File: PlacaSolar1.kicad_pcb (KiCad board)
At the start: 2 copper layers, 32 parts, among them J1 Jack-DC, J2 Conn_01x03_Female, J3 Conn_01x06_Female, J4 Conn_01x15_Female, J5 Conn_01x15_Female, SW1 SW_SPDT, SW2 SW_Push, U1 L78L05_SO8

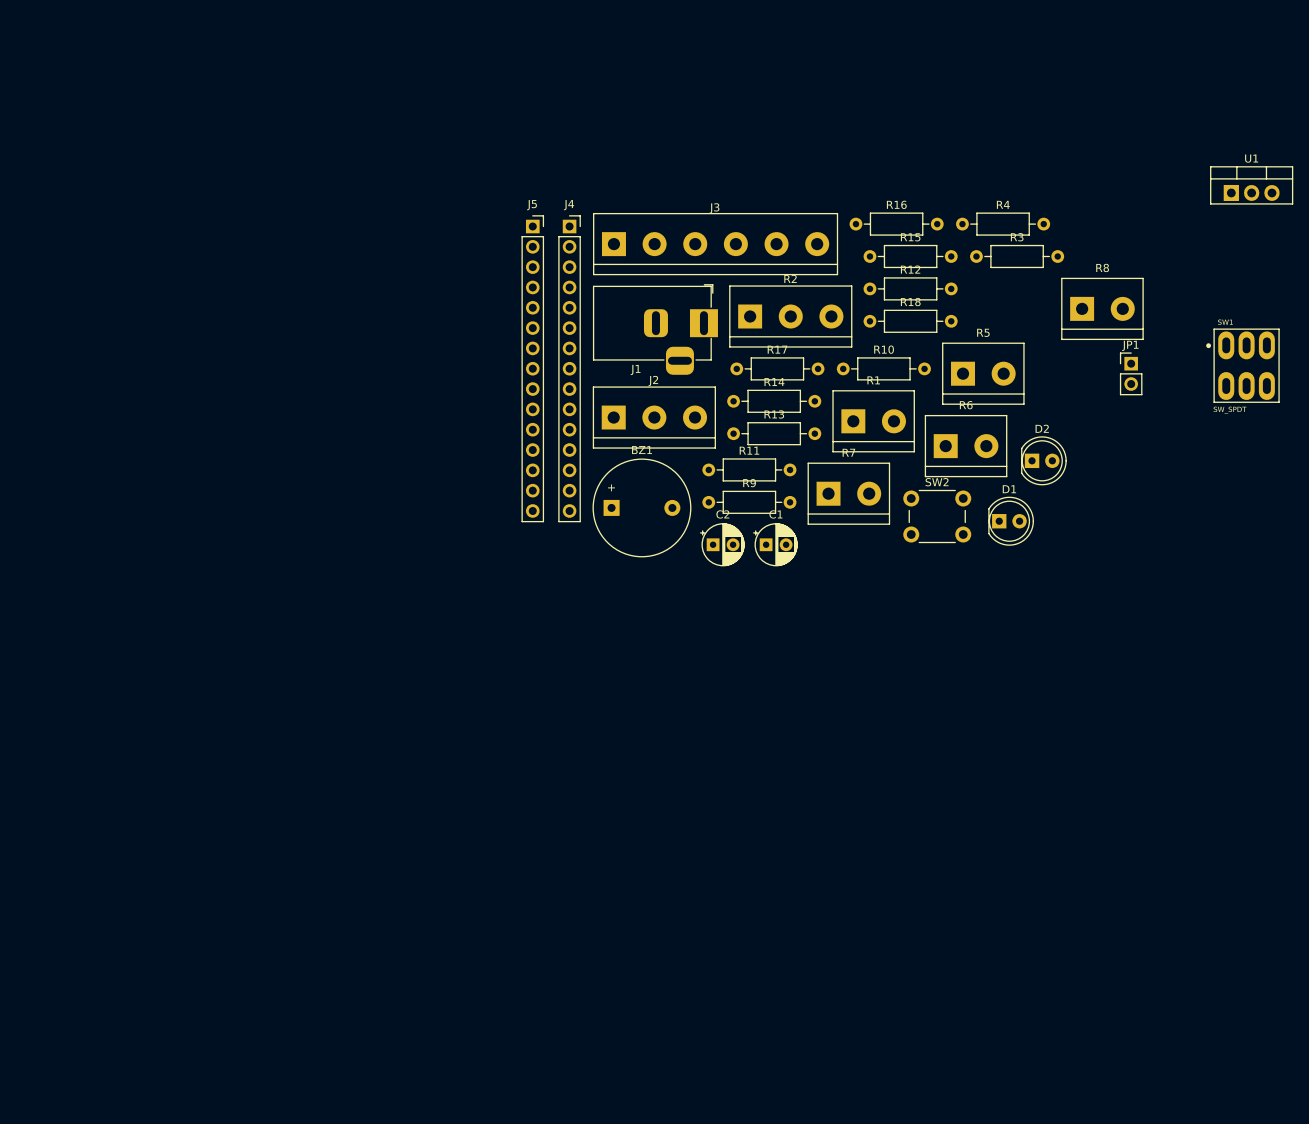
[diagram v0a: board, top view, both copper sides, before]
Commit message: Adicionando modelos 3d, falta o modelo dos bornes, inicio da PCB
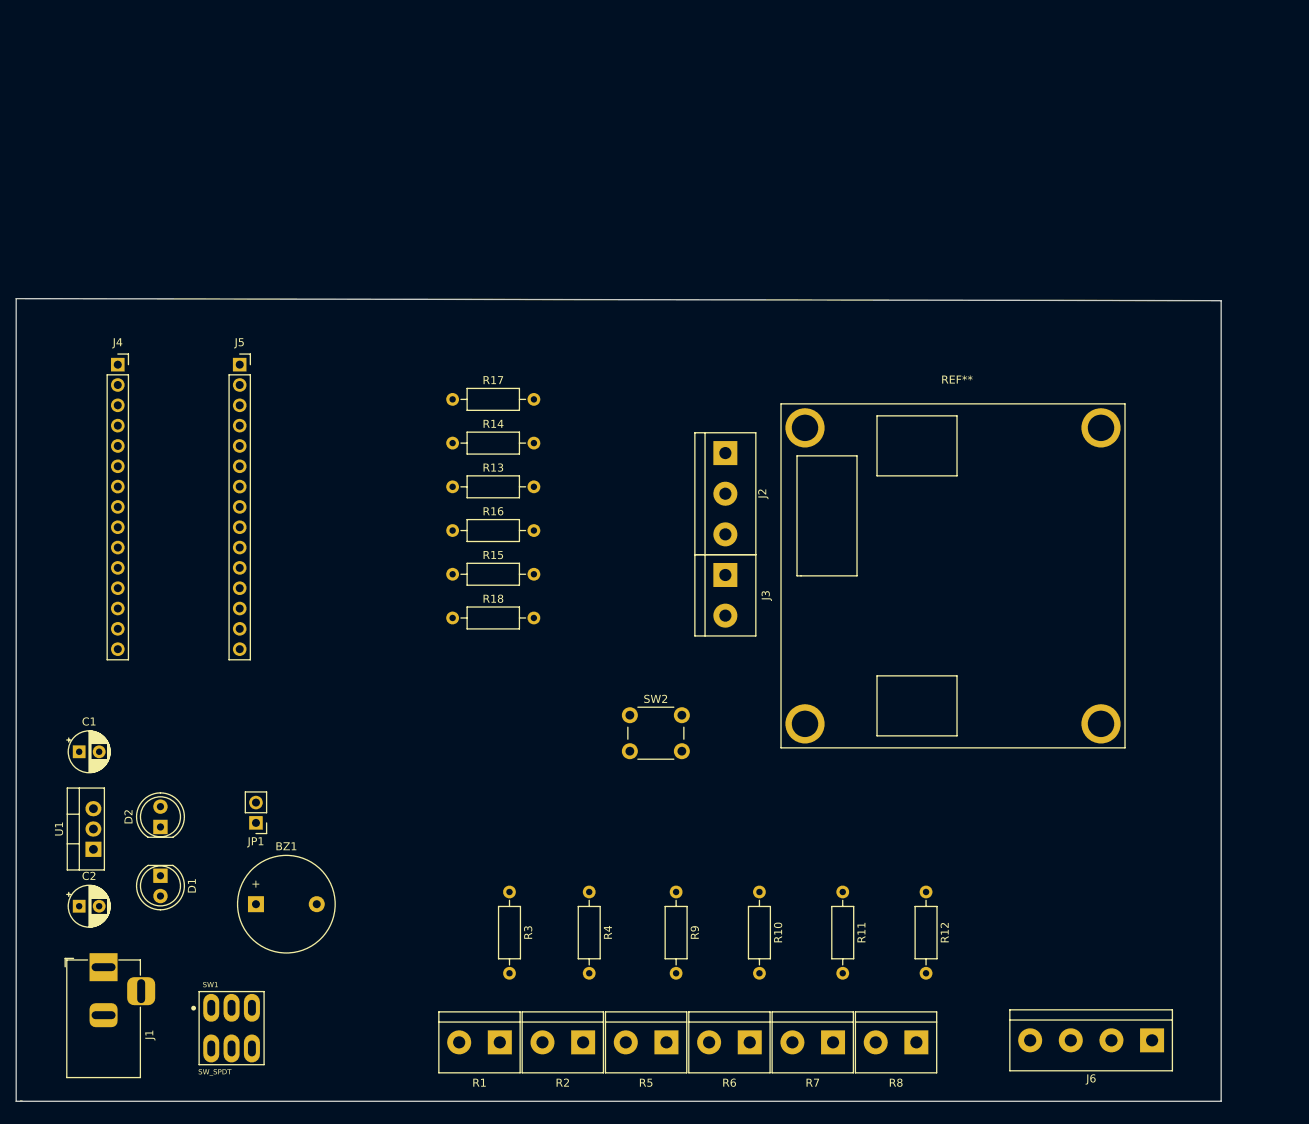
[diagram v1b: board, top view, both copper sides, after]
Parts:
- added J6: Conn_01x04_Female, TerminalBlock:TerminalBlock_bornier-4_P5.08mm, F.Cu at (176.8, 147.8)
- added REF**: ponteH, Painel-Solar:ponteH, F.Cu at (152.4, 64.8)
- J3: value Conn_01x06_Female -> Conn_01x02_Female; footprint TerminalBlock:TerminalBlock_bornier-6_P5.08mm -> TerminalBlock:TerminalBlock_bornier-2_P5.08mm
- R2: footprint TerminalBlock:TerminalBlock_bornier-3_P5.08mm -> TerminalBlock:TerminalBlock_bornier-2_P5.08mm
- moved U1 164.2 mm to (44.5, 124.0), turned to 90 degrees
- moved SW1 151.5 mm to (61.7, 146.3)
- moved JP1 123.5 mm to (64.8, 120.7), turned to 180 degrees
- moved D2 118.2 mm to (52.8, 121.2), turned to 90 degrees
- moved D1 113.8 mm to (52.8, 127.3), turned to 270 degrees
- moved J1 110.1 mm to (45.7, 138.7), turned to 90 degrees
- moved R3 98.6 mm to (96.5, 129.3), turned to 270 degrees
- moved R4 95.6 mm to (106.4, 129.3), turned to 270 degrees
- moved R8 94.0 mm to (147.3, 148.1), turned to 180 degrees
- moved R2 93.1 mm to (105.7, 148.1), turned to 180 degrees
- moved R5 91.4 mm to (116.1, 148.1), turned to 180 degrees
- moved C2 91.2 mm to (42.7, 131.1)
- moved C1 89.7 mm to (42.7, 111.8)
- moved R1 89.3 mm to (95.2, 148.1), turned to 180 degrees
- moved R6 78.5 mm to (126.5, 148.1), turned to 180 degrees
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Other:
- board outline added: 150.6 x 100.3 mm

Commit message: Removendo botão de Reset
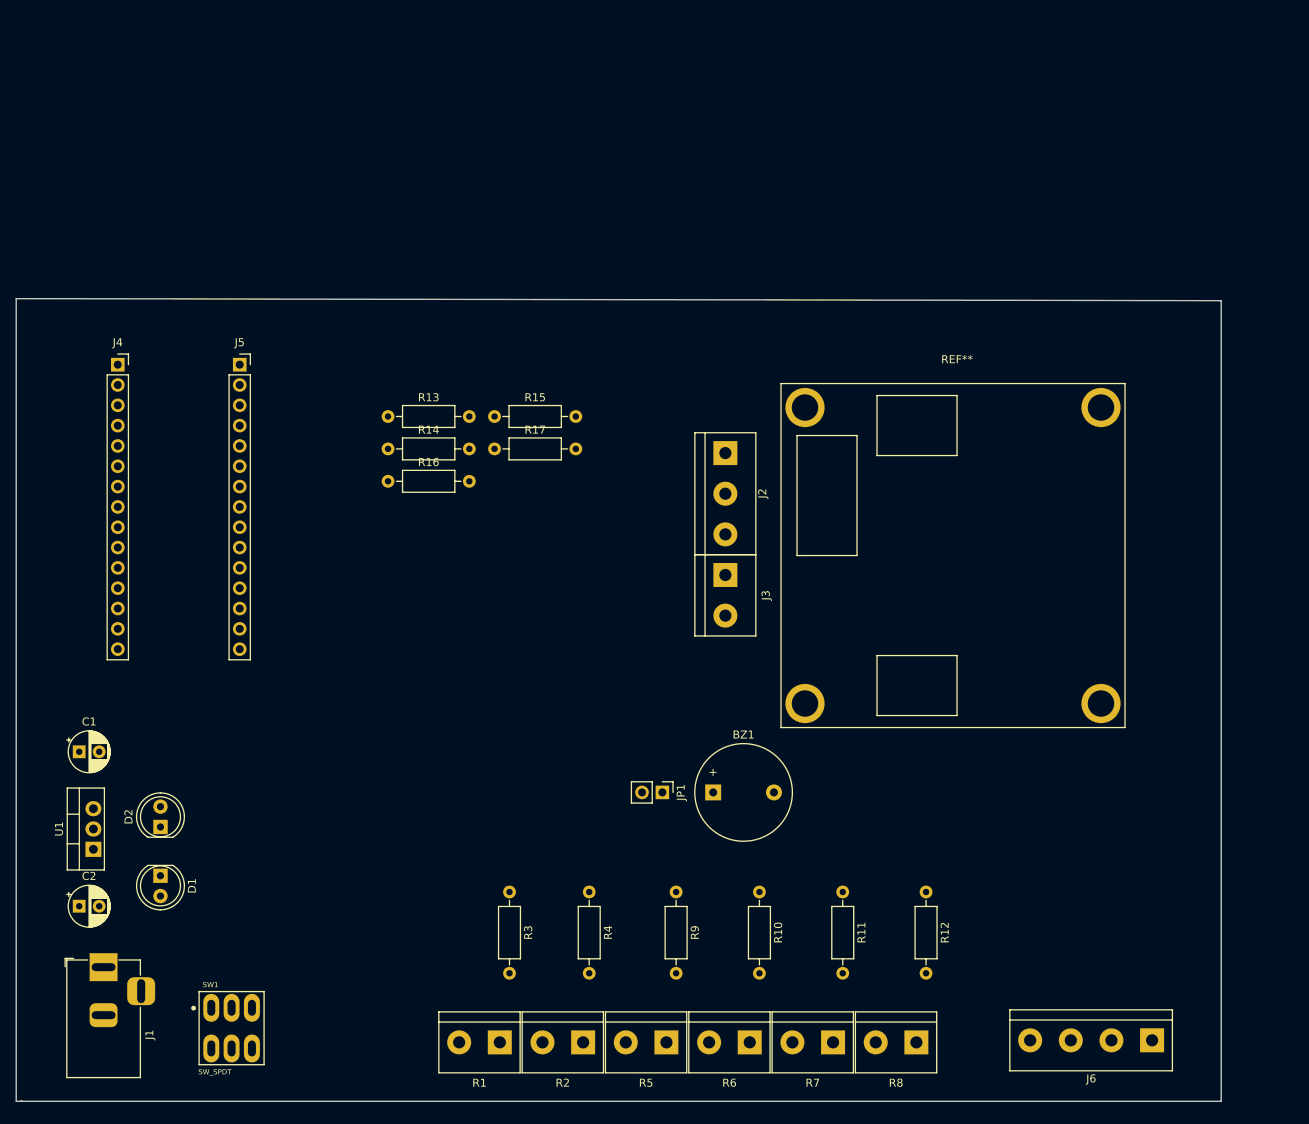
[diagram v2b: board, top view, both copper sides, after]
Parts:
- removed R18: R, Resistor_THT:R_Axial_DIN0207_L6.3mm_D2.5mm_P10.16mm_Horizontal
- removed SW2: SW_Push, Button_Switch_THT:SW_PUSH_6mm
- moved BZ1 58.8 mm to (121.9, 116.8)
- moved JP1 50.9 mm to (115.6, 116.8), turned to 270 degrees
- moved R15 20.4 mm to (94.6, 69.8)
- moved R13 11.9 mm to (81.3, 69.8)
- moved R16 10.1 mm to (81.3, 78.0)
- moved R17 8.11 mm to (94.6, 73.9)
- moved R14 8.10 mm to (81.3, 73.9)
- moved REF** 2.54 mm to (152.4, 62.2)

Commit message: Primeira versão de trilhas da PCB, falta verificar o tamanho de certos componentes
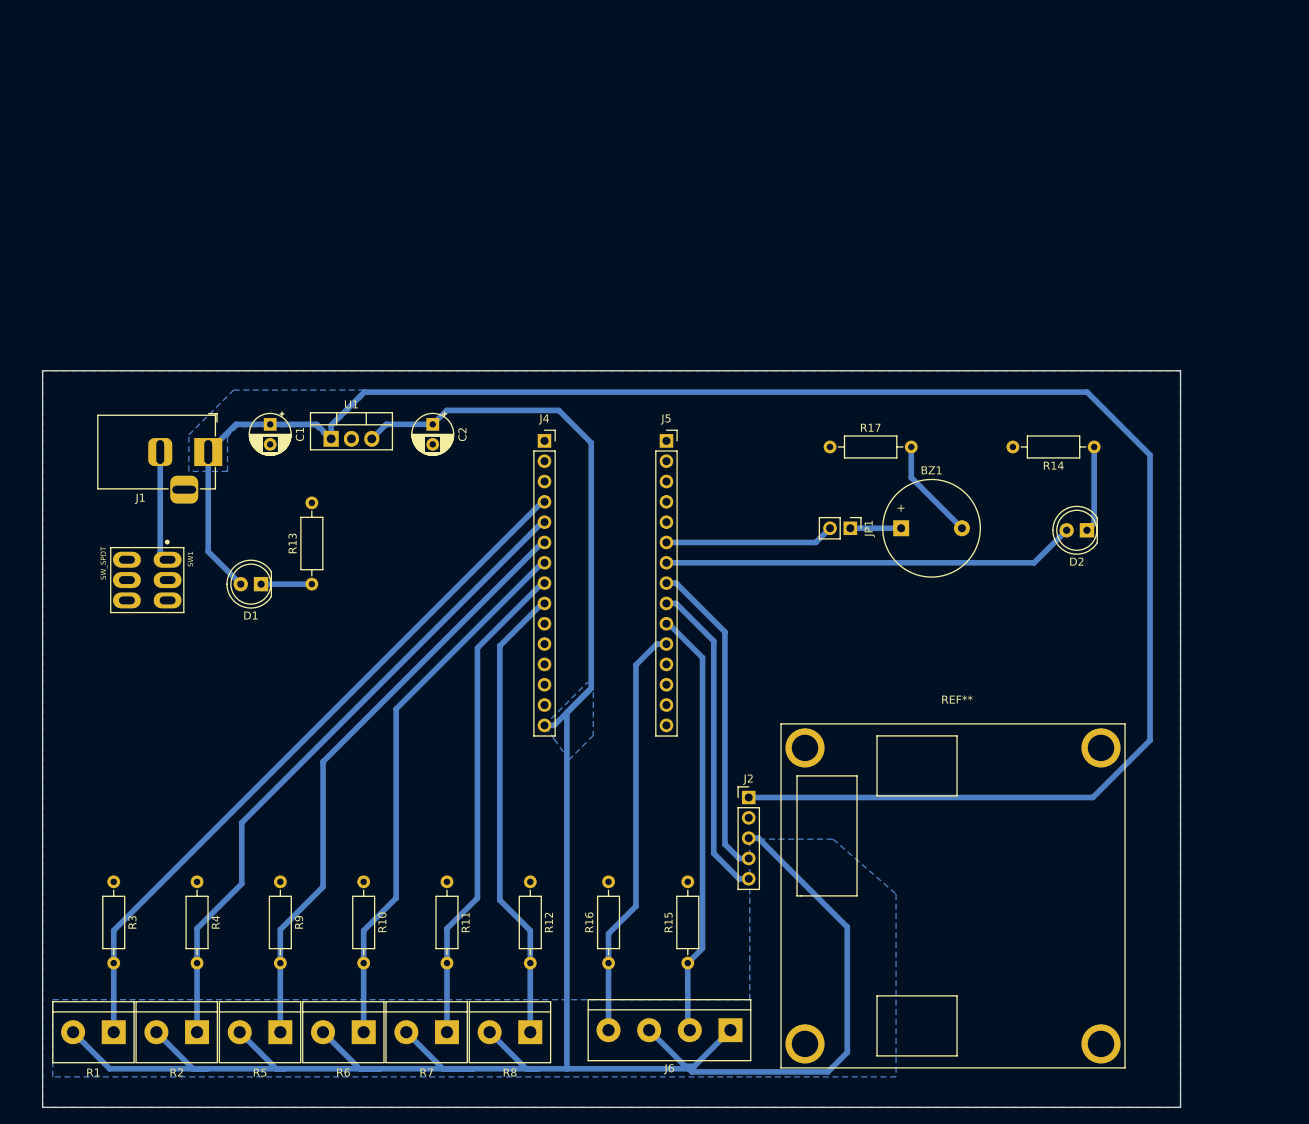
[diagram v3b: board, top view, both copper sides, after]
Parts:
- removed J3: Conn_01x02_Female, TerminalBlock:TerminalBlock_bornier-2_P5.08mm
- J2: value Conn_01x03_Female -> Conn_01x05_Female; footprint TerminalBlock:TerminalBlock_bornier-3_P5.08mm -> Connector_PinHeader_2.54mm:PinHeader_1x05_P2.54mm_Vertical
- U1: value L78L05_SO8 -> L7805
- moved D2 121.6 mm to (168.6, 84.1), turned to 180 degrees
- moved R14 88.3 mm to (169.5, 73.7), turned to 180 degrees
- moved C2 74.7 mm to (86.9, 70.8), turned to 270 degrees
- moved R15 72.5 mm to (118.7, 138.2), turned to 90 degrees
- moved R16 66.2 mm to (108.8, 138.2), turned to 90 degrees
- moved J1 65.7 mm to (58.8, 74.3), turned to 0 degrees
- moved U1 59.3 mm to (74.2, 72.6), turned to 0 degrees
- moved SW1 57.0 mm to (51.2, 90.3), turned to 270 degrees
- moved J5 54.2 mm to (116.1, 72.9)
- moved J4 54.2 mm to (100.8, 72.9)
- moved J6 52.7 mm to (124.1, 146.6)
- moved R11 49.5 mm to (88.6, 128.0)
- moved R10 49.5 mm to (78.2, 128.0)
- moved R12 49.5 mm to (99.1, 128.0)
- moved R9 49.5 mm to (67.8, 128.0)
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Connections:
- U1 pad 1: VIN -> +12V
- U1 pad 3: GND -> VIN
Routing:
- net VIN: track 0.00 -> 307.6 mm
- net +12V: track 0.00 -> 233.6 mm
- net A0: track 0.00 -> 88.8 mm
- net A1: track 0.00 -> 81.9 mm
- net A2: track 0.00 -> 75.1 mm
- net A3: track 0.00 -> 68.2 mm
- net A4: track 0.00 -> 61.3 mm
- net A5: track 0.00 -> 57.6 mm
- net D3: track 0.00 -> 53.7 mm
- net D2: track 0.00 -> 52.0 mm
- net D6: track 0.00 -> 51.7 mm
- net D4: track 0.00 -> 40.1 mm
- net D5: track 0.00 -> 40.1 mm
- net D7: track 0.00 -> 21.2 mm
- net Net-(J1-Pad2): track 0.00 -> 13.8 mm
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- added copper zone on B.Cu, net +12V
- added copper zone on B.Cu, net GND
- added copper zone on B.Cu, net VIN
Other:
- board size 150.6 x 100.3 mm -> 142.2 x 92.1 mm
- net class Alberto added: clearance 0.7, trace_width 0.7, via_dia 0.8, via_drill 0.4

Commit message: Corrigindo disposição dos componentes e das trilhas para caber na pcb de 14x8cm
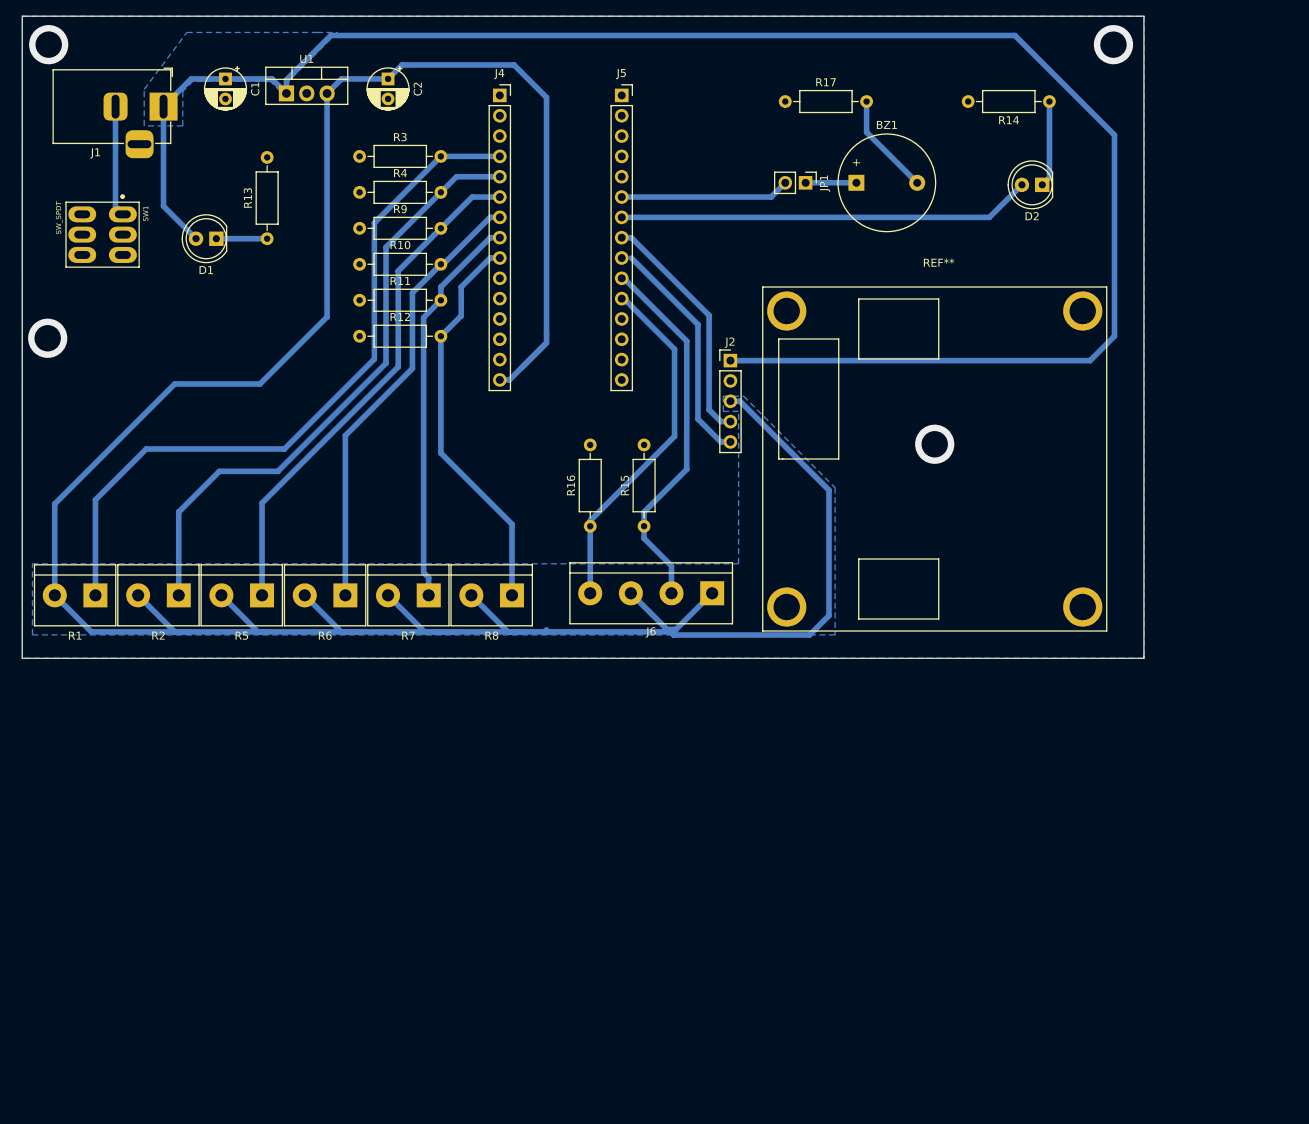
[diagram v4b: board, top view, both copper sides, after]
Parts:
- moved R3 95.7 mm to (77.7, 37.3), turned to 0 degrees
- moved R4 88.5 mm to (77.7, 41.8), turned to 0 degrees
- moved R9 82.3 mm to (77.7, 46.3), turned to 0 degrees
- moved R10 77.2 mm to (77.7, 50.8), turned to 0 degrees
- moved R11 73.5 mm to (77.7, 55.3), turned to 0 degrees
- moved R12 71.5 mm to (77.7, 59.8), turned to 0 degrees
- moved R15 54.9 mm to (113.3, 83.6)
- moved R1 54.7 mm to (44.7, 92.2)
- moved R2 54.7 mm to (55.1, 92.2)
- moved R5 54.7 mm to (65.5, 92.2)
- moved R6 54.7 mm to (75.9, 92.2)
- moved R7 54.7 mm to (86.4, 92.2)
- moved R8 54.7 mm to (96.8, 92.2)
- moved REF** 54.7 mm to (150.1, 50.2)
- moved J6 54.7 mm to (121.8, 91.9)
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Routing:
- net VIN: track 307.6 -> 346.9 mm
- net A3: track 68.2 -> 56.4 mm
- net A4: track 61.3 -> 49.9 mm
- net D4: track 40.1 -> 28.8 mm
- net +12V: track 233.6 -> 222.8 mm
- net A2: track 75.1 -> 64.4 mm
- net D5: track 40.1 -> 30.0 mm
- net A5: track 57.6 -> 49.6 mm
- net D2: track 52.0 -> 44.1 mm
- net D3: track 53.7 -> 46.5 mm
- net A1: track 81.9 -> 76.7 mm
- net A0: track 88.8 -> 90.9 mm
- net (no net): vias 0 -> 4
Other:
- board size 142.2 x 92.1 mm -> 140.2 x 80.3 mm

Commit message: Corrigindo tamanho dos bornes 7x7cm
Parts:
- J6: footprint TerminalBlock:TerminalBlock_bornier-4_P5.08mm -> Painel-Solar:Borne_LAB_4
- R1, R2, R5, R6, R7, R8: footprint TerminalBlock:TerminalBlock_bornier-2_P5.08mm -> Painel-Solar:Borne_LAB_2
- moved R8 11.7 mm to (86.1, 87.4), turned to 0 degrees
- moved J6 11.1 mm to (111.8, 87.1), turned to 0 degrees
- moved R7 8.76 mm to (79.0, 87.4), turned to 0 degrees
- moved R1 7.78 mm to (50.8, 87.4), turned to 0 degrees
- moved R6 6.24 mm to (72.0, 87.4), turned to 0 degrees
- moved R2 5.55 mm to (57.9, 87.4), turned to 0 degrees
- moved R5 4.86 mm to (64.9, 87.4), turned to 0 degrees
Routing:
- net VIN: track 346.9 -> 304.2 mm
- net A0: track 90.9 -> 78.2 mm
- net A1: track 76.7 -> 71.2 mm
- net A5: track 49.6 -> 46.6 mm
- net A4: track 49.9 -> 52.3 mm
- net A3: track 56.4 -> 58.8 mm
- net D2: track 44.1 -> 45.3 mm
- net GND: vias 0 -> 4
- net (no net): vias 4 -> 0
